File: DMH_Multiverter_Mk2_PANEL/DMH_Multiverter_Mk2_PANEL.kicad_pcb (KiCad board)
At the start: 2 copper layers, 50 x 200 mm, 29 parts, among them J0 Panel_GND_Solder_Wire_Pad

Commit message: Added 3rd attenuverter to Panel and Schematic
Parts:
- removed H14, H17: Input, SynthStuff:Jack_6.35mm_Cutout_v3
- removed H15, H16, H18, H19: Output, SynthStuff:Jack_6.35mm_Cutout_Output_v6
- H13: value Output -> Attenuate; footprint SynthStuff:Jack_6.35mm_Cutout_Output_v6 -> SynthStuff:Pot_Cutout_Small_attv_P110KH1
- moved H12 23.9 mm to (58.5, 143.5)
- moved H13 12.2 mm to (83.0, 135.0)
- moved H11 0.25 mm to (58.5, 126.5)
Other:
- board text added: "Attenu verter"
- board text added: "Mk2.0 - March 2025"
- board text added: "SWITCHED MULT"
- board text removed: "Attn & Mult"
- board text removed: "Mk1.0 - December 2024"

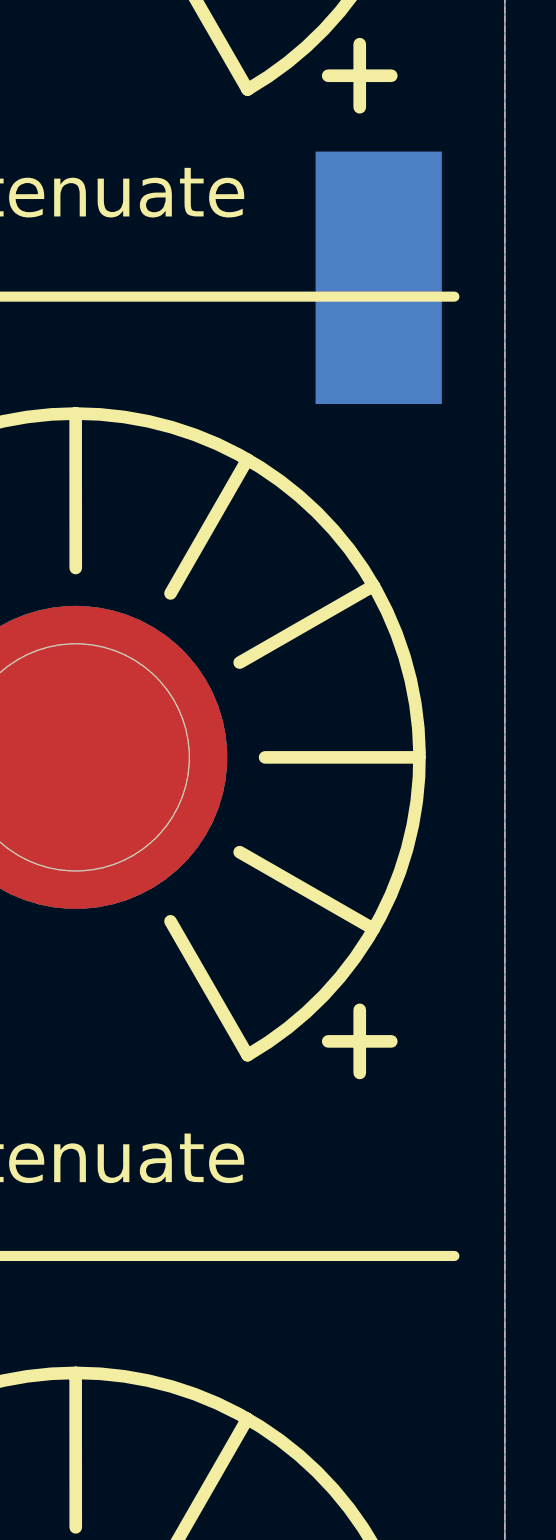
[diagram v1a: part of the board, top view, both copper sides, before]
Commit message: Main PCB components placed
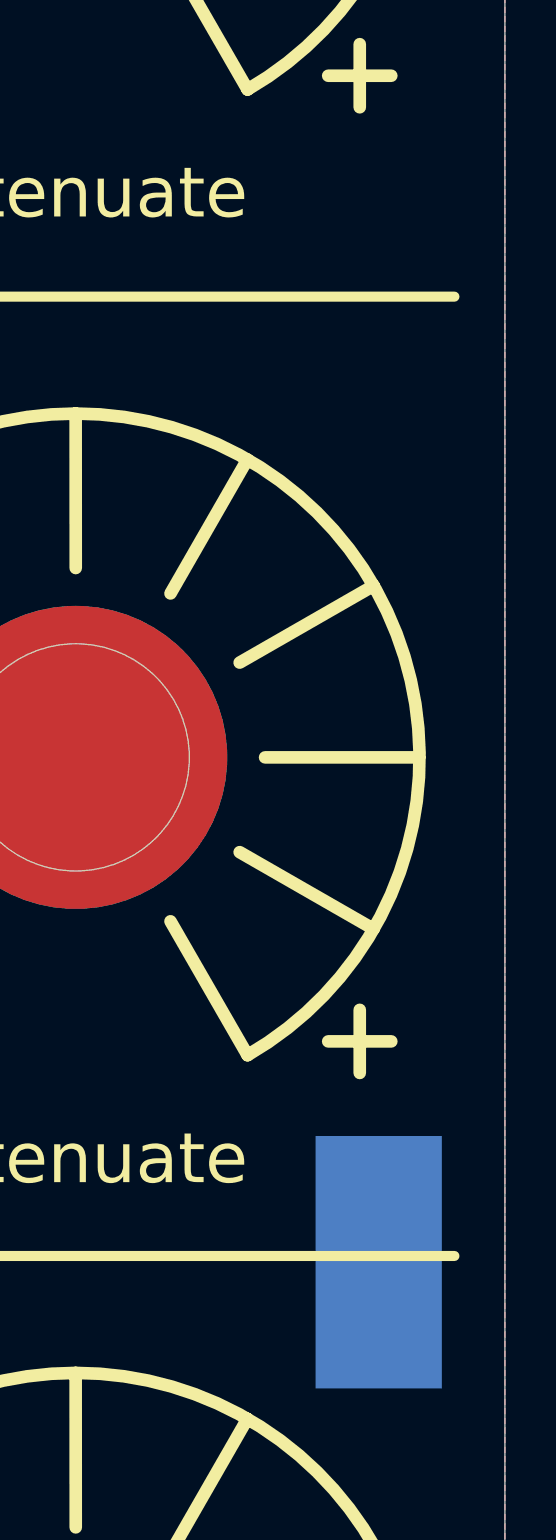
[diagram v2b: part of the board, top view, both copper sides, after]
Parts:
- moved J0 39.0 mm to (95.0, 117.0)
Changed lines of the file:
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@@
 	(footprint "SynthStuff:Panel_GND_SolderWirePad_5x10mm"
 		(layer "B.Cu")
-		(at 95 78 180)
+		(at 95 117 180)
 		(descr "Wire Pad, Square, SMD Pad,  5mm x 10mm,")
 		(tags "MesurementPoint Square SMDPad 5mmx10mm ")

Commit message: pcb 2 in progress
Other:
- board text added: "635"
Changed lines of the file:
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@@
+		)
+	)
+	(gr_text "635"
+		(at 75 225.75 0)
+		(layer "F.SilkS")
+		(effects
+			(font
+				(face "Nulshock Rg")
+				(size 3.5 3.5)
+				(thickness 0.875)
+			)
+		)
+		(render_cache "635" 0
+			(polygon
+				(pts
+					(xy 71.43426 224.02521) (xy 71.354065 224.146839) (xy 70.815082 224.909365) (xy 70.800336 224.943773)
+					(xy 70.815082 224.963221) (xy 70.864316 224.955594) (xy 70.962131 224.938252) (xy 71.101128 224.924998)
+					(xy 71.314742 224.919196) (xy 71.755844 224.919196) (xy 72.011091 224.938841) (xy 72.142759 224.967028)
+					(xy 72.264006 225.006686) (xy 72.378331 225.058751) (xy 72.482477 225.121477) (xy 72.582494 225.198987)
+					(xy 72.67203 225.286782) (xy 72.737639 225.366094) (xy 72.865875 225.580791) (xy 72.944554 225.815867)
+					(xy 72.971013 226.060848) (xy 72.947806 226.292194) (xy 72.915692 226.415232) (xy 72.870808 226.532674)
+					(xy 72.813821 226.643627) (xy 72.745547 226.746865) (xy 72.68076 226.827237) (xy 72.506085 226.984827)
+					(xy 72.29625 227.101879) (xy 72.177069 227.144634) (xy 72.047838 227.176139) (xy 71.907121 227.195786)
+					(xy 71.755844 227.202501) (xy 70.516098 227.202501) (xy 70.231662 227.181826) (xy 70.097253 227.154031)
+					(xy 69.97612 227.115489) (xy 69.86228 227.064418) (xy 69.760339 227.003175) (xy 69.657088 226.922148)
+					(xy 69.565505 226.830213) (xy 69.497718 226.747868) (xy 69.370633 226.534609) (xy 69.292926 226.302962)
+					(xy 69.266735 226.060848) (xy 69.272474 225.992247) (xy 70.212413 225.992247) (xy 70.236443 226.123821)
+					(xy 70.310293 226.24229) (xy 70.33298 226.264504) (xy 70.383882 226.30129) (xy 70.446202 226.329395)
+					(xy 70.526428 226.348307) (xy 70.624023 226.354917) (xy 71.667581 226.354917) (xy 71.703864 226.354089)
+					(xy 71.791011 226.343852) (xy 71.863118 226.322869) (xy 71.928963 226.28781) (xy 71.981311 226.24229)
+					(xy 72.052483 226.130635) (xy 72.079191 225.992247) (xy 72.063633 225.881684) (xy 72.005674 225.771695)
+					(xy 71.960177 225.723109) (xy 71.906648 225.68456) (xy 71.842676 225.65554) (xy 71.762439 225.636241)
+					(xy 71.667581 225.629577) (xy 70.624023 225.629577) (xy 70.54315 225.63432) (xy 70.464403 225.650563)
+					(xy 70.397779 225.677489) (xy 70.336042 225.71911) (xy 70.28593 225.771695) (xy 70.239866 225.848265)
+					(xy 70.219264 225.917605) (xy 70.212413 225.992247) (xy 69.272474 225.992247) (xy 69.283988 225.854606)
+					(xy 69.312272 225.734631) (xy 69.356218 225.611322) (xy 69.426537 225.464979) (xy 69.52148 225.30623)
+					(xy 70.369064 224.005148) (xy 70.423133 223.892521) (xy 71.496183 223.892521)
+				)
+			)
+			(polygon
+				(pts
+					(xy 73.253541 223.892521) (xy 73.253541 224.769811) (xy 75.218414 224.769811) (xy 75.248219 224.776075)
+					(xy 75.266568 224.792569) (xy 75.272269 224.813836) (xy 75.265132 224.842801) (xy 75.242524 224.8653)
+					(xy 75.223116 224.877309) (xy 74.649939 225.239338) (xy 74.548891 225.312924) (xy 74.482456 225.392956)
+					(xy 74.459889 225.447595) (xy 74.44968 225.510779) (xy 74.449049 225.532979) (xy 74.456784 225.61669)
+					(xy 74.483571 225.692267) (xy 74.516676 225.737817) (xy 74.563698 225.775181) (xy 74.619979 225.800559)
+					(xy 74.690649 225.816491) (xy 74.772396 225.821704) (xy 75.438752 225.821704) (xy 75.524511 225.828332)
+					(xy 75.594083 225.847371) (xy 75.645015 225.874956) (xy 75.683895 225.911087) (xy 75.729245 226.005991)
+					(xy 75.737735 226.085853) (xy 75.730581 226.160047) (xy 75.707856 226.225776) (xy 75.676446 226.271436)
+					(xy 75.632371 226.308474) (xy 75.579005 226.334041) (xy 75.512919 226.349876) (xy 75.438752 226.354917)
+					(xy 73.243711 226.354917) (xy 73.243711 227.202501) (xy 75.703328 227.202501) (xy 75.840942 227.195805)
+					(xy 75.96974 227.176288) (xy 76.090146 227.144612) (xy 76.201273 227.101716) (xy 76.397195 226.984015)
+					(xy 76.555436 226.82771) (xy 76.672229 226.637718) (xy 76.7425 226.420777) (xy 76.761846 226.222842)
+					(xy 76.755109 226.083661) (xy 76.735305 225.956213) (xy 76.704266 225.843821) (xy 76.662111 225.742031)
+					(xy 76.610212 225.651874) (xy 76.54858 225.571651) (xy 76.396188 225.438889) (xy 76.202149 225.341452)
+					(xy 75.961329 225.281551) (xy 75.899516 225.273745) (xy 75.875735 225.262473) (xy 75.865761 225.242758)
+					(xy 75.865108 225.234422) (xy 75.884769 225.195313) (xy 76.423752 224.804005) (xy 76.522234 224.71996)
+					(xy 76.597024 224.63178) (xy 76.636424 224.561602) (xy 76.661916 224.485255) (xy 76.673582 224.377649)
+					(xy 76.66675 224.289087) (xy 76.646278 224.206401) (xy 76.614239 224.134393) (xy 76.569961 224.069788)
+					(xy 76.515834 224.015568) (xy 76.450436 223.970064) (xy 76.374606 223.934492) (xy 76.287783 223.909246)
+					(xy 76.119853 223.892521)
+				)
+			)
+			(polygon
+				(pts
+					(xy 77.015309 226.354917) (xy 77.015309 227.202501) (xy 79.680731 227.202501) (xy 79.842095 227.195791)
+					(xy 79.988377 227.176177) (xy 80.116466 227.145572) (xy 80.231686 227.104271) (xy 80.333611 227.053593)
+					(xy 80.4242 226.993823) (xy 80.553105 226.874238) (xy 80.672026 226.69413) (xy 80.749101 226.478773)
+					(xy 80.778264 226.233977) (xy 80.778358 226.218782) (xy 80.771569 226.093472) (xy 80.751398 225.972756)
+					(xy 80.718595 225.858905) (xy 80.673291 225.751468) (xy 80.616987 225.653244) (xy 80.549202 225.563014)
+					(xy 80.430434 225.447707) (xy 80.337589 225.382558) (xy 80.232511 225.327613) (xy 80.122339 225.286523)
+					(xy 79.998306 225.255656) (xy 79.702079 225.227368) (xy 79.671114 225.227156) (xy 78.088359 225.227156)
+					(xy 78.042675 225.219735) (xy 78.021846 225.195143) (xy 78.019757 225.153425) (xy 78.049036 224.828796)
+					(xy 78.060561 224.793563) (xy 78.085278 224.774084) (xy 78.112722 224.769811) (xy 80.655901 224.769811)
+					(xy 80.655901 223.892521) (xy 77.495521 223.892521) (xy 77.409583 223.899344) (xy 77.335707 223.919751)
+					(xy 77.2801 223.949417) (xy 77.234556 223.989798) (xy 77.17592 224.097543) (xy 77.157427 224.211167)
+					(xy 77.08391 225.52614) (xy 77.086882 225.606273) (xy 77.103311 225.673982) (xy 77.129672 225.725601)
+					(xy 77.166123 225.767033) (xy 77.266392 225.819962) (xy 77.38268 225.834741) (xy 79.577935 225.834741)
+					(xy 79.670726 225.841579) (xy 79.744057 225.862096) (xy 79.813019 225.90783) (xy 79.868531 226.000813)
+					(xy 79.88162 226.092478) (xy 79.87491 226.159596) (xy 79.855293 226.217666) (xy 79.813019 226.277125)
+					(xy 79.767719 226.312107) (xy 79.709955 226.337379) (xy 79.577935 226.354917)
+				)
+			)
 		)
 	)
